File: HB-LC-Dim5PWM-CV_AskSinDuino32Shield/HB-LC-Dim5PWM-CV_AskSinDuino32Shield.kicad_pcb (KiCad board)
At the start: 2 copper layers, 73.2 x 37.6 mm, 35 parts, among them J1 power+LED, J2 Encoder 1, J3 Encoder 2, Q11 IRF3708, Q12 IRF3708, Q13 IRF3708, Q14 IRF3708, U1 AskSinDuino32, U2 DS18B20, U3 LC78_05-0.5

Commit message: HB-LC-Dim5PWM-CV_AskSinDuino32Shield
- 5th channel
- SMD FETs
- mounting holes
- PCB size and routing optimized
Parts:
- removed D1, D2, D3, D4: SS16, Diode_SMD:D_SMA
- added H1: MountingHole, MountingHole:MountingHole_3.2mm_M3, F.Cu at (100.7, 59.7)
- added H2: MountingHole, MountingHole:MountingHole_3.5mm, F.Cu at (152.9, 89.2)
- added Q15: IRF8788PbF, Package_SO:SOIC-8_3.9x4.9mm_P1.27mm, F.Cu at (114.8, 90.2)
- added R19: 100R, Resistor_SMD:R_0805_2012Metric_Pad1.20x1.40mm_HandSolder, F.Cu at (123.7, 88.6)
- added R20: 100k, Resistor_SMD:R_0805_2012Metric_Pad1.20x1.40mm_HandSolder, F.Cu at (123.7, 90.7)
- JP1: value direct 3V3 -> direct_3V3
- Q11, Q12, Q13, Q14: value IRF3708 -> IRF8788PbF; footprint Package_TO_SOT_THT:TO-220-3_Vertical -> Package_SO:SOIC-8_3.9x4.9mm_P1.27mm
- moved Q11 21.4 mm to (114.8, 67.8), turned to 180 degrees
- moved R12 15.9 mm to (123.7, 73.2)
- moved R11 15.9 mm to (123.7, 71.1)
- moved C2 14.6 mm to (124.7, 58.9)
- moved R18 13.2 mm to (123.7, 86.6)
- moved R17 13.2 mm to (123.7, 84.6)
- moved Q14 11.5 mm to (114.8, 84.6), turned to 180 degrees
- moved Q12 10.9 mm to (114.8, 73.4), turned to 180 degrees
- moved J1 9.99 mm to (103.4, 78.4)
- moved U3 9.32 mm to (113.8, 61.3), turned to 0 degrees
- moved C25 8.98 mm to (125.2, 67.8), turned to -90 degrees
- moved C1 7.67 mm to (108.0, 59.8)
- moved J3 6.71 mm to (153.7, 73.2)
- moved U2 6.55 mm to (121.2, 65.5), turned to -90 degrees
- moved J2 6.47 mm to (153.7, 59.2)
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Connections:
- J1 pad 1: /LED1 -> /LED5
- J1 pad 2: /LED2 -> /LED4
- J1 pad 4: /LED4 -> /LED2
- J1 pad 5: +24V -> /LED1
- J1 pad 7: GND -> +24V
- Q11 pad 1: /LED1 -> GND
- Q11 pad 2: Net-(Q11-G) -> GND
- Q12 pad 1: /LED2 -> GND
- Q12 pad 2: Net-(Q12-G) -> GND
- Q13 pad 1: /LED3 -> GND
- Q13 pad 2: Net-(Q13-G) -> GND
- Q14 pad 1: /LED4 -> GND
- Q14 pad 2: Net-(Q14-G) -> GND
- U1 pad W11: /1WIRE -> unconnected-(U1-PA2-PadW11)
- U1 pad W12: unconnected-(U1-PA1-PadW12) -> /1WIRE
- U1 pad W4: unconnected-(U1-PB1-PadW4) -> /PWM5
- U1 pad W5: unconnected-(U1-PB0-PadW5) -> /PWM4
- U1 pad W6: /PWM1 -> /PWM3
- U1 pad W8: /PWM3 -> /PWM1
- U1 pad W9: /PWM4 -> unconnected-(U1-PA4-PadW9)
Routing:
- net GND: track 32.1 -> 61.3 mm, vias 7 -> 24
- net /LED5: track 0.00 -> 14.3 mm
- net /LED4: track 20.8 -> 9.68 mm
- net +5V: track 51.4 -> 40.6 mm
- net /LED3: track 25.3 -> 15.5 mm
- net Net-(Q15-G): track 0.00 -> 7.59 mm
- net /LED2: track 19.6 -> 12.1 mm
- net /PWM1: track 10.6 -> 4.01 mm
- net /PWM5: track 0.00 -> 6.36 mm
- net /1WIRE: track 14.4 -> 8.65 mm
- net /LED1: track 24.1 -> 18.7 mm
- net Net-(J2-Pin_2): track 7.15 -> 12.3 mm
- net /PWM2: track 8.58 -> 3.69 mm
- net Net-(J2-Pin_1): track 6.13 -> 9.56 mm
- net /DATA2: track 6.72 -> 3.32 mm
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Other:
- board size 73.2 x 37.6 mm -> 62 x 37.4 mm
- board text added: "LED5| 4 | 3 | 2 | 1 | +24V |GND|"
- board text removed: "LED1| 2 | 3 | 4 | +24V | GND |"

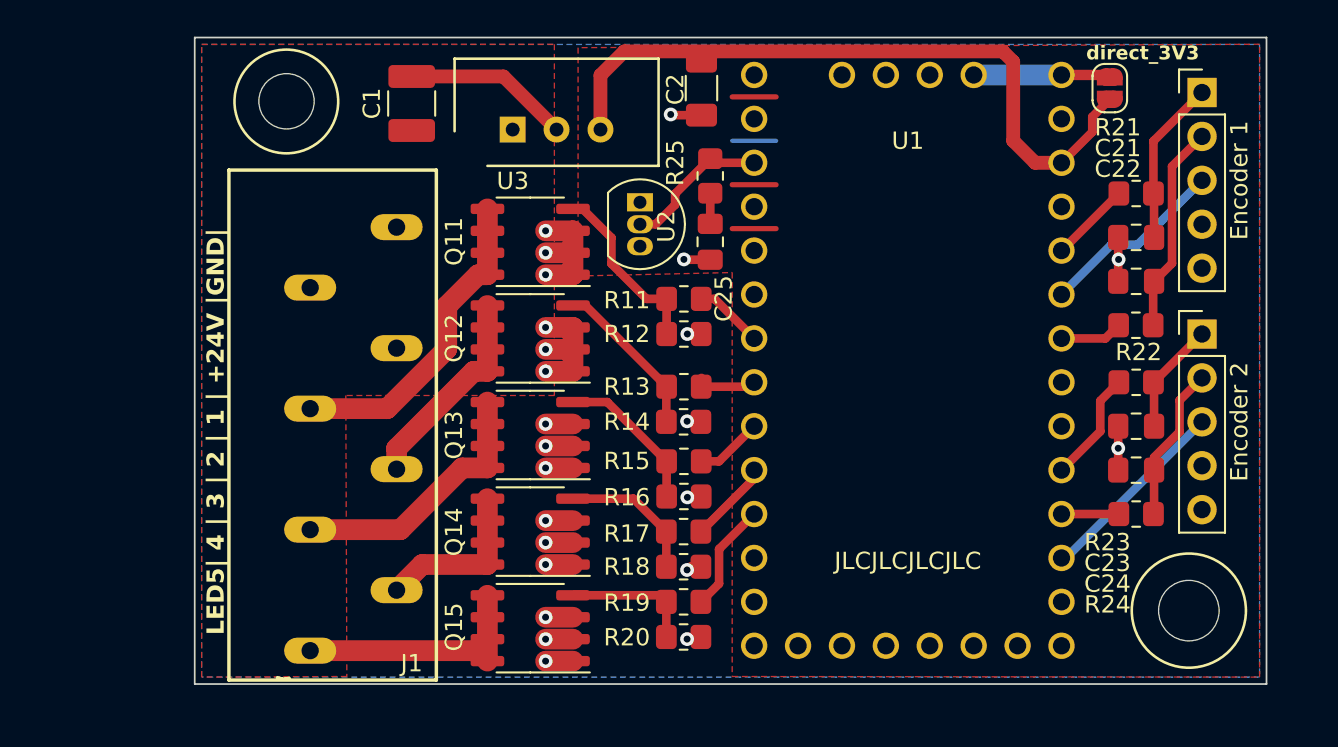
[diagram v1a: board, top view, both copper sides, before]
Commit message: small improvements in supply layer
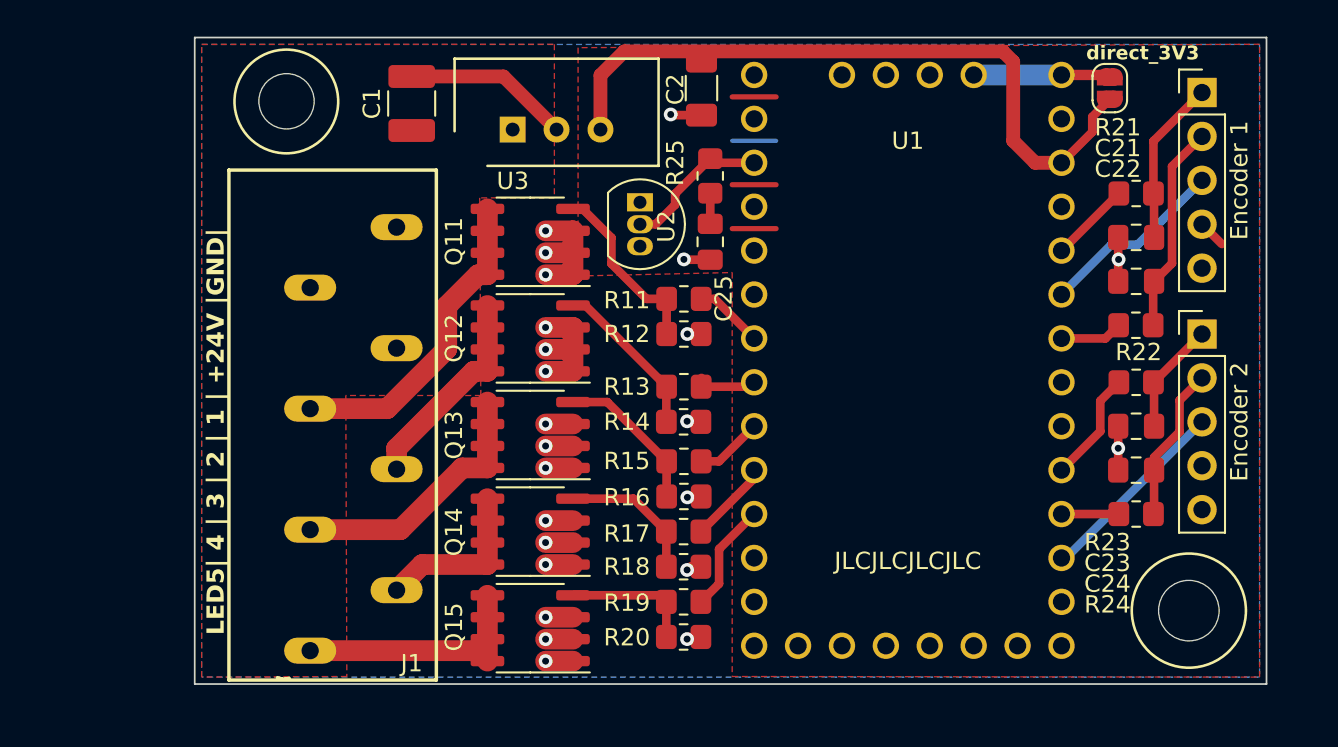
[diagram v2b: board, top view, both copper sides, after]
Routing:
- net +3V3: track 17.2 -> 18.8 mm
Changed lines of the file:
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@@
     (fp_line (start 1.6 1.25) (end -1.6 1.25)
       (stroke (width 0.1) (type solid)) (layer "F.Fab"))
-    (pad "1" smd roundrect (at -1.5625 0 90) (size 1.325 2.7) (layers "F.Cu" "F.Paste" "F.Mask") (roundrect_rratio 0.188679)
+    (pad "1" smd roundrect (at -1.5625 0 90) (size 1.325 2.7) (layers "F.Cu" "F.Paste" "F.Mask") (roundrect_rratio 0.1886792453)
       (net 28 "+24V") (pintype "passive"))
-    (pad "2" smd roundrect (at 1.5625 0 90) (size 1.325 2.7) (layers "F.Cu" "F.Paste" "F.Mask") (roundrect_rratio 0.188679)
+    (pad "2" smd roundrect (at 1.5625 0 90) (size 1.325 2.7) (layers "F.Cu" "F.Paste" "F.Mask") (roundrect_rratio 0.1886792453)
       (net 6 "GND") (pintype "passive"))
     (model "${KICAD6_3DMODEL_DIR}/Capacitor_SMD.3dshapes/C_1210_3225Metric.wrl"
@@
     (fp_line (start 1 0.625) (end -1 0.625)
       (stroke (width 0.1) (type solid)) (layer "F.Fab"))
-    (pad "1" smd roundrect (at -1 0 180) (size 1.2 1.4) (layers "F.Cu" "F.Paste" "F.Mask") (roundrect_rratio 0.208333)
+    (pad "1" smd roundrect (at -1 0 180) (size 1.2 1.4) (layers "F.Cu" "F.Paste" "F.Mask") (roundrect_rratio 0.2083333333)
       (net 6 "GND") (pintype "passive"))
-    (pad "2" smd roundrect (at 1 0 180) (size 1.2 1.4) (layers "F.Cu" "F.Paste" "F.Mask") (roundrect_rratio 0.208333)
+    (pad "2" smd roundrect (at 1 0 180) (size 1.2 1.4) (layers "F.Cu" "F.Paste" "F.Mask") (roundrect_rratio 0.2083333333)
       (net 42 "Net-(Q15-G)") (pintype "passive"))
     (model "${KICAD6_3DMODEL_DIR}/Resistor_SMD.3dshapes/R_0805_2012Metric.wrl"
@@
     (fp_line (start 1 0.625) (end -1 0.625)
       (stroke (width 0.1) (type solid)) (layer "F.Fab"))
-    (pad "1" smd roundrect (at -1 0 180) (size 1.2 1.4) (layers "F.Cu" "F.Paste" "F.Mask") (roundrect_rratio 0.208333)
+    (pad "1" smd roundrect (at -1 0 180) (size 1.2 1.4) (layers "F.Cu" "F.Paste" "F.Mask") (roundrect_rratio 0.2083333333)
       (net 43 "/PWM5") (pintype "passive"))
-    (pad "2" smd roundrect (at 1 0 180) (size 1.2 1.4) (layers "F.Cu" "F.Paste" "F.Mask") (roundrect_rratio 0.208333)
+    (pad "2" smd roundrect (at 1 0 180) (size 1.2 1.4) (layers "F.Cu" "F.Paste" "F.Mask") (roundrect_rratio 0.2083333333)
       (net 42 "Net-(Q15-G)") (pintype "passive"))
     (model "${KICAD6_3DMODEL_DIR}/Resistor_SMD.3dshapes/R_0805_2012Metric.wrl"
@@
   (segment (start 126.492 64.516) (end 129.032 64.516) (width 0.3) (layer "F.Cu") (net 9))
   (segment (start 126.492 59.436) (end 129.032 59.436) (width 0.3) (layer "F.Cu") (net 9))
+  (segment (start 153.67 66.802) (end 154.813 67.945) (width 0.5) (layer "F.Cu") (net 9))
   (segment (start 145.542 58.166) (end 140.462 58.166) (width 1.2) (layer "B.Cu") (net 9))
   (segment (start 150.86 61.992) (end 153.67 59.182) (width 0.5) (layer "F.Cu") (net 11))
@@
         (xy 95.8 56.4)
         (xy 116.205 56.388)
-        (xy 116.205 76.708)
+        (xy 116.205 65.278)
+        (xy 111.887 65.278)
+        (xy 111.9505 76.708)
         (xy 104.14 76.708)
         (xy 104.2 92.964)
